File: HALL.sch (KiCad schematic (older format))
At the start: 1 part, among them P6 CON_HALL

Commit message: i think im good with the schematics
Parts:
- added C?: 10nF, symbol C_Small
- added R?: 50kR, symbol R_Small
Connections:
- net GND: now also C?.2
- net HALL_U: now also C?.1, R?.1
- net VCC renamed +5V
- new net HALL_PWM: R?.2
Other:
- moved on the sheet: P6
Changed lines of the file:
@@
 $Descr A4 11693 8268
 encoding utf-8
-Sheet 12 12
+Sheet 9 12
 Title ""
 Date ""
@@
 L CONN_01X05 P6
 U 1 1 57ADAAC3
-P 1300 950
-F 0 "P6" H 1300 1250 50  0000 C CNN
-F 1 "CON_HALL" V 1400 950 50  0000 C CNN
-F 2 "Terminal_Blocks:TerminalBlock_Pheonix_MPT-2.54mm_5pol" H 1300 950 50  0001 C CNN
-F 3 "" H 1300 950 50  0000 C CNN
-	1    1300 950
+P 2300 1700
+F 0 "P6" H 2300 2000 50  0000 C CNN
+F 1 "CON_HALL" V 2400 1700 50  0000 C CNN
+F 2 "Terminal_Blocks:TerminalBlock_Pheonix_MPT-2.54mm_5pol" H 2300 1700 50  0001 C CNN
+F 3 "" H 2300 1700 50  0000 C CNN
+	1    2300 1700
 	1    0    0    1
 $EndComp
 Wire Wire Line
-	1000 650  1000 750
+	2000 1400 2000 1500
 Wire Wire Line
-	1000 750  1100 750
+	2000 1500 2100 1500
 $Comp
 L GND #PWR049
 U 1 1 57ADAB3C
-P 1000 1250
-F 0 "#PWR049" H 1000 1000 50  0001 C CNN
-F 1 "GND" H 1000 1100 50  0000 C CNN
-F 2 "" H 1000 1250 50  0000 C CNN
-F 3 "" H 1000 1250 50  0000 C CNN
-	1    1000 1250
+P 2000 2000
+F 0 "#PWR049" H 2000 1750 50  0001 C CNN
+F 1 "GND" H 2000 1850 50  0000 C CNN
+F 2 "" H 2000 2000 50  0000 C CNN
+F 3 "" H 2000 2000 50  0000 C CNN
+	1    2000 2000
 	1    0    0    -1
 $EndComp
 Wire Wire Line
-	1000 1250 1000 1150
+	2000 2000 2000 1900
 Wire Wire Line
-	1000 1150 1100 1150
-Text HLabel 1000 850  0    60   Output ~ 0
+	2000 1900 2100 1900
+Text HLabel 1750 1600 0    60   Output ~ 0
 HALL_U
-Text HLabel 1000 950  0    60   Output ~ 0
+Text HLabel 1750 1700 0    60   Output ~ 0
 HALL_V
-Text HLabel 1000 1050 0    60   Output ~ 0
+Text HLabel 1750 1800 0    60   Output ~ 0
 HALL_W
-Wire Wire Line
-	1000 1050 1100 1050
-Wire Wire Line
-	1100 950  1000 950
-Wire Wire Line
-	1000 850  1100 850
 $Comp
-L VCC #PWR050
-U 1 1 57B357EE
-P 1000 650
-F 0 "#PWR050" H 1000 500 50  0001 C CNN
-F 1 "VCC" H 1000 800 50  0000 C CNN
-F 2 "" H 1000 650 50  0000 C CNN
-F 3 "" H 1000 650 50  0000 C CNN
-	1    1000 650
+L +5V #PWR?
+U 1 1 580F5FAC
+P 2000 1400
+F 0 "#PWR?" H 2000 1250 50  0001 C CNN
+F 1 "+5V" H 2000 1540 50  0000 C CNN
+F 2 "" H 2000 1400 50  0000 C CNN
+F 3 "" H 2000 1400 50  0000 C CNN
+	1    2000 1400
 	1    0    0    -1
 $EndComp
+$Comp
+L C_Small C?
+U 1 1 580F6E53
+P 1800 2250
+F 0 "C?" H 1810 2320 50  0000 L CNN
+F 1 "10nF" H 1700 2150 50  0000 L CNN
+F 2 "" H 1800 2250 50  0000 C CNN
+F 3 "" H 1800 2250 50  0000 C CNN
+	1    1800 2250
+	1    0    0    -1
+$EndComp
+$Comp
+L GND #PWR?
+U 1 1 580F6E9B
+P 1800 2450
+F 0 "#PWR?" H 1800 2200 50  0001 C CNN
+F 1 "GND" H 1800 2300 50  0000 C CNN
+F 2 "" H 1800 2450 50  0000 C CNN
+F 3 "" H 1800 2450 50  0000 C CNN
+	1    1800 2450
+	1    0    0    -1
+$EndComp
+$Comp
+L R_Small R?
+U 1 1 580F71C7
+P 1600 1950
+F 0 "R?" V 1550 1900 50  0000 L CNN
+F 1 "50kR" V 1650 1900 50  0000 L CNN
+F 2 "" H 1600 1950 50  0000 C CNN
+F 3 "" H 1600 1950 50  0000 C CNN
+	1    1600 1950
+	0    1    1    0
+$EndComp
+Wire Wire Line
+	1750 1600 2100 1600
+Wire Wire Line
+	1750 1700 2100 1700
+Wire Wire Line
+	1750 1800 2100 1800
+Wire Wire Line
+	1800 2350 1800 2450
+Text HLabel 1450 1950 0    60   Input ~ 0
+HALL_PWM
+Wire Wire Line
+	1450 1950 1500 1950
+Wire Wire Line
+	1700 1950 1800 1950
+Wire Wire Line
+	1800 1600 1800 2150
+Connection ~ 1800 1600
+Connection ~ 1800 1950
 $EndSCHEMATC

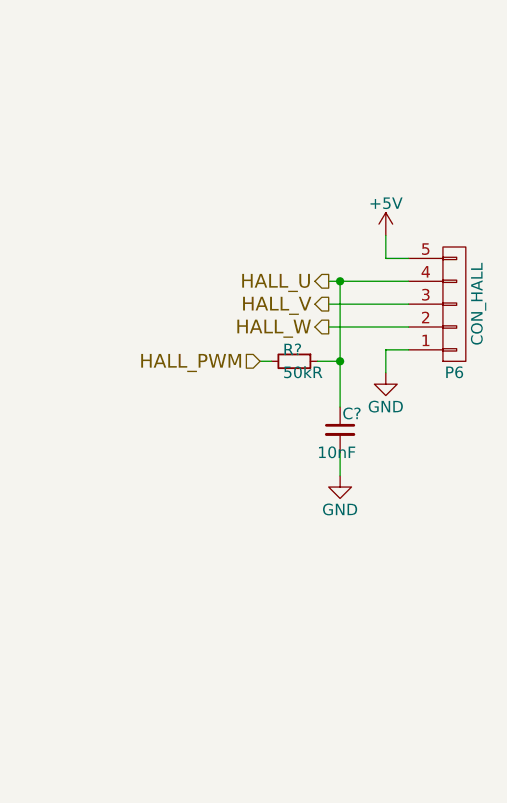
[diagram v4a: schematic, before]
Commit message: changed the maximum outpul voltage of the RC-Filter to VPP
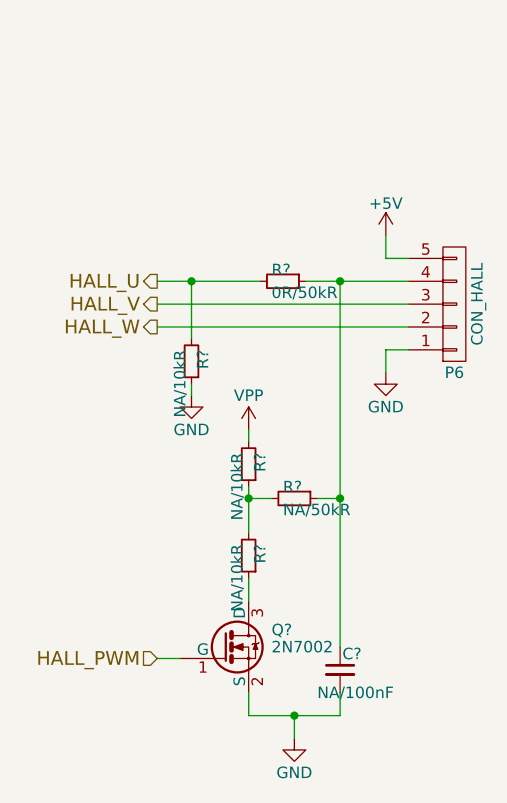
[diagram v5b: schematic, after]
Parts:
- added Q?: 2N7002, TO_SOT_Packages_SMD:SOT-23, symbol 2N7002
- added R?: 0R/50kR, symbol R_Small
- added R? (x3): NA/10kR, symbol R_Small
- C?: value 10nF -> NA/100nF
- R?: value 50kR -> NA/50kR
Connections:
- net GND: now also Q?.2 (S), R?.1
- net HALL_PWM: now also Q?.1 (G); no longer R?.2
- net HALL_U: now also R?.2, R?.2; no longer C?.1, P6.4 (P4), R?.1
- new net: C?.1, P6.4 (P4), R?.1, R?.1
- new net: Q?.3 (D), R?.1
- new net: R?.1, R?.2, R?.2
- new net VPP: R?.2
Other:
- moved on the sheet: C?, R?
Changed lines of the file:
@@
 $Descr A4 11693 8268
 encoding utf-8
-Sheet 9 12
+Sheet 12 12
 Title ""
 Date ""
@@
 Wire Wire Line
 	2000 1900 2100 1900
-Text HLabel 1750 1600 0    60   Output ~ 0
+Text HLabel 1000 1600 0    60   Output ~ 0
 HALL_U
-Text HLabel 1750 1700 0    60   Output ~ 0
+Text HLabel 1000 1700 0    60   Output ~ 0
 HALL_V
-Text HLabel 1750 1800 0    60   Output ~ 0
+Text HLabel 1000 1800 0    60   Output ~ 0
 HALL_W
 $Comp
@@
 L C_Small C?
 U 1 1 580F6E53
-P 1800 2250
-F 0 "C?" H 1810 2320 50  0000 L CNN
-F 1 "10nF" H 1700 2150 50  0000 L CNN
-F 2 "" H 1800 2250 50  0000 C CNN
-F 3 "" H 1800 2250 50  0000 C CNN
-	1    1800 2250
+P 1800 3300
+F 0 "C?" H 1810 3370 50  0000 L CNN
+F 1 "NA/100nF" H 1700 3200 50  0000 L CNN
+F 2 "" H 1800 3300 50  0000 C CNN
+F 3 "" H 1800 3300 50  0000 C CNN
+	1    1800 3300
 	1    0    0    -1
 $EndComp
@@
 L GND #PWR?
 U 1 1 580F6E9B
-P 1800 2450
-F 0 "#PWR?" H 1800 2200 50  0001 C CNN
-F 1 "GND" H 1800 2300 50  0000 C CNN
-F 2 "" H 1800 2450 50  0000 C CNN
-F 3 "" H 1800 2450 50  0000 C CNN
-	1    1800 2450
+P 1600 3600
+F 0 "#PWR?" H 1600 3350 50  0001 C CNN
+F 1 "GND" H 1600 3450 50  0000 C CNN
+F 2 "" H 1600 3600 50  0000 C CNN
+F 3 "" H 1600 3600 50  0000 C CNN
+	1    1600 3600
 	1    0    0    -1
 $EndComp
@@
 L R_Small R?
 U 1 1 580F71C7
-P 1600 1950
-F 0 "R?" V 1550 1900 50  0000 L CNN
-F 1 "50kR" V 1650 1900 50  0000 L CNN
-F 2 "" H 1600 1950 50  0000 C CNN
-F 3 "" H 1600 1950 50  0000 C CNN
-	1    1600 1950
+P 1600 2550
+F 0 "R?" V 1550 2500 50  0000 L CNN
+F 1 "NA/50kR" V 1650 2500 50  0000 L CNN
+F 2 "" H 1600 2550 50  0000 C CNN
+F 3 "" H 1600 2550 50  0000 C CNN
+	1    1600 2550
 	0    1    1    0
 $EndComp
 Wire Wire Line
-	1750 1600 2100 1600
-Wire Wire Line
-	1750 1700 2100 1700
-Wire Wire Line
-	1750 1800 2100 1800
-Wire Wire Line
-	1800 2350 1800 2450
-Text HLabel 1450 1950 0    60   Input ~ 0
+	1650 1600 2100 1600
+Wire Wire Line
+	1000 1700 2100 1700
+Text HLabel 1000 3250 0    60   Input ~ 0
 HALL_PWM
 Wire Wire Line
-	1450 1950 1500 1950
-Wire Wire Line
-	1700 1950 1800 1950
-Wire Wire Line
-	1800 1600 1800 2150
+	1700 2550 1800 2550
+Wire Wire Line
+	1800 1600 1800 3200
 Connection ~ 1800 1600
-Connection ~ 1800 1950
+Connection ~ 1800 2550
+Wire Wire Line
+	1000 1800 2100 1800
+$Comp
+L R_Small R?
+U 1 1 580F173E
+P 1550 1600
+F 0 "R?" V 1500 1550 50  0000 L CNN
+F 1 "0R/50kR" V 1600 1550 50  0000 L CNN
+F 2 "" H 1550 1600 50  0000 C CNN
+F 3 "" H 1550 1600 50  0000 C CNN
+	1    1550 1600
+	0    1    1    0
+$EndComp
+Wire Wire Line
+	1000 1600 1450 1600
+$Comp
+L R_Small R?
+U 1 1 580F1844
+P 1150 1950
+F 0 "R?" V 1100 1900 50  0000 L CNN
+F 1 "NA/10kR" V 1200 1900 50  0000 L CNN
+F 2 "" H 1150 1950 50  0000 C CNN
+F 3 "" H 1150 1950 50  0000 C CNN
+	1    1150 1950
+	-1   0    0    1
+$EndComp
+Wire Wire Line
+	1150 1850 1150 1600
+Connection ~ 1150 1600
+$Comp
+L VPP #PWR?
+U 1 1 580F18F3
+P 1400 2250
+F 0 "#PWR?" H 1400 2100 50  0001 C CNN
+F 1 "VPP" H 1400 2400 50  0000 C CNN
+F 2 "" H 1400 2250 50  0000 C CNN
+F 3 "" H 1400 2250 50  0000 C CNN
+	1    1400 2250
+	1    0    0    -1
+$EndComp
+$Comp
+L 2N7002 Q?
+U 1 1 580F19BB
+P 1300 3200
+F 0 "Q?" H 1500 3275 50  0000 L CNN
+F 1 "2N7002" H 1500 3200 50  0000 L CNN
+F 2 "TO_SOT_Packages_SMD:SOT-23" H 1500 3125 50  0001 L CIN
+F 3 "" H 1300 3200 50  0000 L CNN
+	1    1300 3200
+	1    0    0    -1
+$EndComp
+Wire Wire Line
+	1400 3400 1400 3500
+Wire Wire Line
+	1400 3500 1800 3500
+Wire Wire Line
+	1800 3500 1800 3400
+Wire Wire Line
+	1600 3600 1600 3500
+Connection ~ 1600 3500
+$Comp
+L R_Small R?
+U 1 1 580F1ACA
+P 1400 2400
+F 0 "R?" V 1350 2350 50  0000 L CNN
+F 1 "NA/10kR" V 1450 2350 50  0000 L CNN
+F 2 "" H 1400 2400 50  0000 C CNN
+F 3 "" H 1400 2400 50  0000 C CNN
+	1    1400 2400
+	-1   0    0    1
+$EndComp
+Wire Wire Line
+	1400 2250 1400 2300
+Wire Wire Line
+	1500 2550 1400 2550
+Wire Wire Line
+	1400 2500 1400 2700
+Connection ~ 1400 2550
+Wire Wire Line
+	1000 3250 1100 3250
+$Comp
+L GND #PWR?
+U 1 1 580F1E73
+P 1150 2100
+F 0 "#PWR?" H 1150 1850 50  0001 C CNN
+F 1 "GND" H 1150 1950 50  0000 C CNN
+F 2 "" H 1150 2100 50  0000 C CNN
+F 3 "" H 1150 2100 50  0000 C CNN
+	1    1150 2100
+	1    0    0    -1
+$EndComp
+Wire Wire Line
+	1150 2100 1150 2050
+$Comp
+L R_Small R?
+U 1 1 580F218F
+P 1400 2800
+F 0 "R?" V 1350 2750 50  0000 L CNN
+F 1 "NA/10kR" V 1450 2750 50  0000 L CNN
+F 2 "" H 1400 2800 50  0000 C CNN
+F 3 "" H 1400 2800 50  0000 C CNN
+	1    1400 2800
+	-1   0    0    1
+$EndComp
+Wire Wire Line
+	1400 2900 1400 3000
 $EndSCHEMATC

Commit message: routed... at least for now
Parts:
- removed R?: NA/10kR, symbol R_Small
- C24: renamed from C?; footprint (none) -> Capacitors_SMD:C_0603
- R15, R16, R17, R18: renamed from R?; footprint (none) -> Resistors_SMD:R_0603
- gave numbers to parts that had none: 1
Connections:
- net at Q7.3 (D): now also R16.1, R18.2
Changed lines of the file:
@@
 	2000 1500 2100 1500
 $Comp
-L GND #PWR049
+L GND #PWR052
 U 1 1 57ADAB3C
 P 2000 2000
-F 0 "#PWR049" H 2000 1750 50  0001 C CNN
+F 0 "#PWR052" H 2000 1750 50  0001 C CNN
 F 1 "GND" H 2000 1850 50  0000 C CNN
 F 2 "" H 2000 2000 50  0000 C CNN
@@
 HALL_W
 $Comp
-L +5V #PWR?
+L +5V #PWR053
 U 1 1 580F5FAC
 P 2000 1400
-F 0 "#PWR?" H 2000 1250 50  0001 C CNN
+F 0 "#PWR053" H 2000 1250 50  0001 C CNN
 F 1 "+5V" H 2000 1540 50  0000 C CNN
 F 2 "" H 2000 1400 50  0000 C CNN
@@
 $EndComp
 $Comp
-L C_Small C?
+L C_Small C24
 U 1 1 580F6E53
 P 1800 3300
-F 0 "C?" H 1810 3370 50  0000 L CNN
+F 0 "C24" H 1810 3370 50  0000 L CNN
 F 1 "NA/100nF" H 1700 3200 50  0000 L CNN
-F 2 "" H 1800 3300 50  0000 C CNN
+F 2 "Capacitors_SMD:C_0603" H 1800 3300 50  0001 C CNN
 F 3 "" H 1800 3300 50  0000 C CNN
 	1    1800 3300
@@
 $EndComp
 $Comp
-L GND #PWR?
+L GND #PWR054
 U 1 1 580F6E9B
 P 1600 3600
-F 0 "#PWR?" H 1600 3350 50  0001 C CNN
+F 0 "#PWR054" H 1600 3350 50  0001 C CNN
 F 1 "GND" H 1600 3450 50  0000 C CNN
 F 2 "" H 1600 3600 50  0000 C CNN
@@
 $EndComp
 $Comp
-L R_Small R?
+L R_Small R18
 U 1 1 580F71C7
 P 1600 2550
-F 0 "R?" V 1550 2500 50  0000 L CNN
+F 0 "R18" V 1550 2500 50  0000 L CNN
 F 1 "NA/50kR" V 1650 2500 50  0000 L CNN
-F 2 "" H 1600 2550 50  0000 C CNN
+F 2 "Resistors_SMD:R_0603" H 1600 2550 50  0001 C CNN
 F 3 "" H 1600 2550 50  0000 C CNN
 	1    1600 2550
@@
 	1000 1800 2100 1800
 $Comp
-L R_Small R?
+L R_Small R17
 U 1 1 580F173E
 P 1550 1600
-F 0 "R?" V 1500 1550 50  0000 L CNN
+F 0 "R17" V 1500 1550 50  0000 L CNN
 F 1 "0R/50kR" V 1600 1550 50  0000 L CNN
-F 2 "" H 1550 1600 50  0000 C CNN
+F 2 "Resistors_SMD:R_0603" H 1550 1600 50  0001 C CNN
 F 3 "" H 1550 1600 50  0000 C CNN
 	1    1550 1600
@@
 	1000 1600 1450 1600
 $Comp
-L R_Small R?
+L R_Small R15
 U 1 1 580F1844
 P 1150 1950
-F 0 "R?" V 1100 1900 50  0000 L CNN
+F 0 "R15" V 1100 1900 50  0000 L CNN
 F 1 "NA/10kR" V 1200 1900 50  0000 L CNN
-F 2 "" H 1150 1950 50  0000 C CNN
+F 2 "Resistors_SMD:R_0603" H 1150 1950 50  0001 C CNN
 F 3 "" H 1150 1950 50  0000 C CNN
 	1    1150 1950
@@
 Connection ~ 1150 1600
 $Comp
-L VPP #PWR?
+L VPP #PWR055
 U 1 1 580F18F3
 P 1400 2250
-F 0 "#PWR?" H 1400 2100 50  0001 C CNN
+F 0 "#PWR055" H 1400 2100 50  0001 C CNN
 F 1 "VPP" H 1400 2400 50  0000 C CNN
 F 2 "" H 1400 2250 50  0000 C CNN
@@
 $EndComp
 $Comp
-L 2N7002 Q?
+L 2N7002 Q7
 U 1 1 580F19BB
 P 1300 3200
-F 0 "Q?" H 1500 3275 50  0000 L CNN
+F 0 "Q7" H 1500 3275 50  0000 L CNN
 F 1 "2N7002" H 1500 3200 50  0000 L CNN
 F 2 "TO_SOT_Packages_SMD:SOT-23" H 1500 3125 50  0001 L CIN
@@
 Connection ~ 1600 3500
 $Comp
-L R_Small R?
+L R_Small R16
 U 1 1 580F1ACA
 P 1400 2400
-F 0 "R?" V 1350 2350 50  0000 L CNN
+F 0 "R16" V 1350 2350 50  0000 L CNN
 F 1 "NA/10kR" V 1450 2350 50  0000 L CNN
-F 2 "" H 1400 2400 50  0000 C CNN
+F 2 "Resistors_SMD:R_0603" H 1400 2400 50  0001 C CNN
 F 3 "" H 1400 2400 50  0000 C CNN
 	1    1400 2400
@@
 	1500 2550 1400 2550
 Wire Wire Line
-	1400 2500 1400 2700
+	1400 2500 1400 3000
 Connection ~ 1400 2550
 Wire Wire Line
 	1000 3250 1100 3250
 $Comp
-L GND #PWR?
+L GND #PWR056
 U 1 1 580F1E73
 P 1150 2100
-F 0 "#PWR?" H 1150 1850 50  0001 C CNN
+F 0 "#PWR056" H 1150 1850 50  0001 C CNN
 F 1 "GND" H 1150 1950 50  0000 C CNN
 F 2 "" H 1150 2100 50  0000 C CNN
@@
 Wire Wire Line
 	1150 2100 1150 2050
-$Comp
-L R_Small R?
-U 1 1 580F218F
-P 1400 2800
-F 0 "R?" V 1350 2750 50  0000 L CNN
-F 1 "NA/10kR" V 1450 2750 50  0000 L CNN
-F 2 "" H 1400 2800 50  0000 C CNN
-F 3 "" H 1400 2800 50  0000 C CNN
-	1    1400 2800
-	-1   0    0    1
-$EndComp
-Wire Wire Line
-	1400 2900 1400 3000
 $EndSCHEMATC

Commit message: long forgotten commit of something I did half a year ago -.-
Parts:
- removed C24: NA/100nF, Capacitors_SMD:C_0603, symbol C_Small
- removed Q7: 2N7002, TO_SOT_Packages_SMD:SOT-23, symbol 2N7002
- removed R15, R16: NA/10kR, Resistors_SMD:R_0603, symbol R_Small
- removed R17: 0R/50kR, Resistors_SMD:R_0603, symbol R_Small
- removed R18: NA/50kR, Resistors_SMD:R_0603, symbol R_Small
- added R16, R17, R18: 47kR, Resistor_SMD:R_0603_1608Metric, symbol bldc-controller-rescue:R_Small
- P6: footprint Terminal_Blocks:TerminalBlock_Pheonix_MPT-2.54mm_5pol -> Connector_PinHeader_2.54mm:PinHeader_1x05_P2.54mm_Horizontal; symbol CONN_01X05 -> bldc-controller-rescue:CONN_01X05
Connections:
- net labels removed: GND, HALL_PWM, VPP
- wire segments 20 -> 18
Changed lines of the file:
@@
-EESchema Schematic File Version 2
-LIBS:bldc-controller-rescue
-LIBS:power
-LIBS:device
-LIBS:transistors
-LIBS:conn
-LIBS:linear
-LIBS:regul
-LIBS:74xx
-LIBS:cmos4000
-LIBS:adc-dac
-LIBS:memory
-LIBS:xilinx
-LIBS:microcontrollers
-LIBS:dsp
-LIBS:microchip
-LIBS:analog_switches
-LIBS:motorola
-LIBS:texas
-LIBS:intel
-LIBS:audio
-LIBS:interface
-LIBS:digital-audio
-LIBS:philips
-LIBS:display
-LIBS:cypress
-LIBS:siliconi
-LIBS:opto
-LIBS:atmel
-LIBS:contrib
-LIBS:valves
-LIBS:Power_Management
-LIBS:st-microelectronics
-LIBS:stm32
-LIBS:w_analog
-LIBS:mpu6000
+EESchema Schematic File Version 4
 LIBS:bldc-controller-cache
-EELAYER 25 0
+EELAYER 29 0
 EELAYER END
 $Descr A4 11693 8268
@@
 $EndDescr
 $Comp
-L CONN_01X05 P6
+L bldc-controller-rescue:CONN_01X05 P6
 U 1 1 57ADAAC3
 P 2300 1700
 F 0 "P6" H 2300 2000 50  0000 C CNN
 F 1 "CON_HALL" V 2400 1700 50  0000 C CNN
-F 2 "Terminal_Blocks:TerminalBlock_Pheonix_MPT-2.54mm_5pol" H 2300 1700 50  0001 C CNN
+F 2 "Connector_PinHeader_2.54mm:PinHeader_1x05_P2.54mm_Horizontal" H 2300 1700 50  0001 C CNN
 F 3 "" H 2300 1700 50  0000 C CNN
 	1    2300 1700
-	1    0    0    1
+	1    0    0    -1
 $EndComp
 Wire Wire Line
@@
 Wire Wire Line
 	2000 1500 2100 1500
-$Comp
-L GND #PWR052
-U 1 1 57ADAB3C
-P 2000 2000
-F 0 "#PWR052" H 2000 1750 50  0001 C CNN
-F 1 "GND" H 2000 1850 50  0000 C CNN
-F 2 "" H 2000 2000 50  0000 C CNN
-F 3 "" H 2000 2000 50  0000 C CNN
-	1    2000 2000
-	1    0    0    -1
-$EndComp
-Wire Wire Line
-	2000 2000 2000 1900
 Wire Wire Line
 	2000 1900 2100 1900
@@
 HALL_W
 $Comp
-L +5V #PWR053
+L bldc-controller-rescue:+5V #PWR053
 U 1 1 580F5FAC
 P 2000 1400
+AR Path="/580F5FAC" Ref="#PWR053"  Part="1"
+AR Path="/580FABC4/580F5FAC" Ref="#PWR053"  Part="1"
 F 0 "#PWR053" H 2000 1250 50  0001 C CNN
 F 1 "+5V" H 2000 1540 50  0000 C CNN
@@
 	1    0    0    -1
 $EndComp
+Wire Wire Line
+	1000 1700 1550 1700
+Wire Wire Line
+	1000 1800 1700 1800
 $Comp
-L C_Small C24
-U 1 1 580F6E53
-P 1800 3300
-F 0 "C24" H 1810 3370 50  0000 L CNN
-F 1 "NA/100nF" H 1700 3200 50  0000 L CNN
-F 2 "Capacitors_SMD:C_0603" H 1800 3300 50  0001 C CNN
-F 3 "" H 1800 3300 50  0000 C CNN
-	1    1800 3300
-	1    0    0    -1
+L bldc-controller-rescue:R_Small R16
+U 1 1 5D30EF33
+P 1400 1250
+F 0 "R16" V 1350 1200 50  0000 L CNN
+F 1 "47kR" V 1450 1200 50  0000 L CNN
+F 2 "Resistor_SMD:R_0603_1608Metric" H 1400 1250 50  0001 C CNN
+F 3 "" H 1400 1250 50  0000 C CNN
+	1    1400 1250
+	-1   0    0    1
 $EndComp
 $Comp
-L GND #PWR054
-U 1 1 580F6E9B
-P 1600 3600
-F 0 "#PWR054" H 1600 3350 50  0001 C CNN
-F 1 "GND" H 1600 3450 50  0000 C CNN
-F 2 "" H 1600 3600 50  0000 C CNN
-F 3 "" H 1600 3600 50  0000 C CNN
-	1    1600 3600
-	1    0    0    -1
+L bldc-controller-rescue:R_Small R17
+U 1 1 5D30F3A9
+P 1550 1250
+F 0 "R17" V 1500 1200 50  0000 L CNN
+F 1 "47kR" V 1600 1200 50  0000 L CNN
+F 2 "Resistor_SMD:R_0603_1608Metric" H 1550 1250 50  0001 C CNN
+F 3 "" H 1550 1250 50  0000 C CNN
+	1    1550 1250
+	-1   0    0    1
 $EndComp
 $Comp
-L R_Small R18
-U 1 1 580F71C7
-P 1600 2550
-F 0 "R18" V 1550 2500 50  0000 L CNN
-F 1 "NA/50kR" V 1650 2500 50  0000 L CNN
-F 2 "Resistors_SMD:R_0603" H 1600 2550 50  0001 C CNN
-F 3 "" H 1600 2550 50  0000 C CNN
-	1    1600 2550
-	0    1    1    0
-$EndComp
-Wire Wire Line
-	1650 1600 2100 1600
-Wire Wire Line
-	1000 1700 2100 1700
-Text HLabel 1000 3250 0    60   Input ~ 0
-HALL_PWM
-Wire Wire Line
-	1700 2550 1800 2550
-Wire Wire Line
-	1800 1600 1800 3200
-Connection ~ 1800 1600
-Connection ~ 1800 2550
-Wire Wire Line
-	1000 1800 2100 1800
-$Comp
-L R_Small R17
-U 1 1 580F173E
-P 1550 1600
-F 0 "R17" V 1500 1550 50  0000 L CNN
-F 1 "0R/50kR" V 1600 1550 50  0000 L CNN
-F 2 "Resistors_SMD:R_0603" H 1550 1600 50  0001 C CNN
-F 3 "" H 1550 1600 50  0000 C CNN
-	1    1550 1600
-	0    1    1    0
-$EndComp
-Wire Wire Line
-	1000 1600 1450 1600
-$Comp
-L R_Small R15
-U 1 1 580F1844
-P 1150 1950
-F 0 "R15" V 1100 1900 50  0000 L CNN
-F 1 "NA/10kR" V 1200 1900 50  0000 L CNN
-F 2 "Resistors_SMD:R_0603" H 1150 1950 50  0001 C CNN
-F 3 "" H 1150 1950 50  0000 C CNN
-	1    1150 1950
+L bldc-controller-rescue:R_Small R18
+U 1 1 5D30F5F4
+P 1700 1250
+F 0 "R18" V 1650 1200 50  0000 L CNN
+F 1 "47kR" V 1750 1200 50  0000 L CNN
+F 2 "Resistor_SMD:R_0603_1608Metric" H 1700 1250 50  0001 C CNN
+F 3 "" H 1700 1250 50  0000 C CNN
+	1    1700 1250
 	-1   0    0    1
 $EndComp
 Wire Wire Line
-	1150 1850 1150 1600
-Connection ~ 1150 1600
+	1400 1350 1400 1600
+Connection ~ 1400 1600
+Wire Wire Line
+	1400 1600 2100 1600
+Wire Wire Line
+	1550 1350 1550 1700
+Connection ~ 1550 1700
+Wire Wire Line
+	1550 1700 2100 1700
+Wire Wire Line
+	1700 1350 1700 1800
+Connection ~ 1700 1800
+Wire Wire Line
+	1700 1800 2100 1800
 $Comp
-L VPP #PWR055
-U 1 1 580F18F3
-P 1400 2250
-F 0 "#PWR055" H 1400 2100 50  0001 C CNN
-F 1 "VPP" H 1400 2400 50  0000 C CNN
-F 2 "" H 1400 2250 50  0000 C CNN
-F 3 "" H 1400 2250 50  0000 C CNN
-	1    1400 2250
-	1    0    0    -1
-$EndComp
-$Comp
-L 2N7002 Q7
-U 1 1 580F19BB
-P 1300 3200
-F 0 "Q7" H 1500 3275 50  0000 L CNN
-F 1 "2N7002" H 1500 3200 50  0000 L CNN
-F 2 "TO_SOT_Packages_SMD:SOT-23" H 1500 3125 50  0001 L CIN
-F 3 "" H 1300 3200 50  0000 L CNN
-	1    1300 3200
+L bldc-controller-rescue:+5V #PWR?
+U 1 1 5D30FE82
+P 1550 900
+AR Path="/5D30FE82" Ref="#PWR?"  Part="1"
+AR Path="/580FABC4/5D30FE82" Ref="#PWR0101"  Part="1"
+F 0 "#PWR0101" H 1550 750 50  0001 C CNN
+F 1 "+5V" H 1550 1040 50  0000 C CNN
+F 2 "" H 1550 900 50  0000 C CNN
+F 3 "" H 1550 900 50  0000 C CNN
+	1    1550 900
 	1    0    0    -1
 $EndComp
 Wire Wire Line
-	1400 3400 1400 3500
+	1550 900  1550 1000
 Wire Wire Line
-	1400 3500 1800 3500
+	1400 1150 1400 1000
 Wire Wire Line
-	1800 3500 1800 3400
+	1400 1000 1550 1000
+Connection ~ 1550 1000
 Wire Wire Line
-	1600 3600 1600 3500
-Connection ~ 1600 3500
-$Comp
-L R_Small R16
-U 1 1 580F1ACA
-P 1400 2400
-F 0 "R16" V 1350 2350 50  0000 L CNN
-F 1 "NA/10kR" V 1450 2350 50  0000 L CNN
-F 2 "Resistors_SMD:R_0603" H 1400 2400 50  0001 C CNN
-F 3 "" H 1400 2400 50  0000 C CNN
-	1    1400 2400
-	-1   0    0    1
-$EndComp
+	1550 1000 1550 1150
 Wire Wire Line
-	1400 2250 1400 2300
+	1700 1150 1700 1000
 Wire Wire Line
-	1500 2550 1400 2550
+	1700 1000 1550 1000
 Wire Wire Line
-	1400 2500 1400 3000
-Connection ~ 1400 2550
-Wire Wire Line
-	1000 3250 1100 3250
-$Comp
-L GND #PWR056
-U 1 1 580F1E73
-P 1150 2100
-F 0 "#PWR056" H 1150 1850 50  0001 C CNN
-F 1 "GND" H 1150 1950 50  0000 C CNN
-F 2 "" H 1150 2100 50  0000 C CNN
-F 3 "" H 1150 2100 50  0000 C CNN
-	1    1150 2100
-	1    0    0    -1
-$EndComp
-Wire Wire Line
-	1150 2100 1150 2050
+	1000 1600 1400 1600
 $EndSCHEMATC
